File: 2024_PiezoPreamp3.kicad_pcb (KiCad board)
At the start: 4 copper layers, 71 x 36.8 mm, 91 parts, among them J101 6.3mm stereo, J102 6.3mm stereo, J201 DC IN 5.5/2.1mm, J401 Spring Contact, U101 OPA145, U102 OPA145, U201 ZXMP3A17E6TA, U301 BC847BS,115

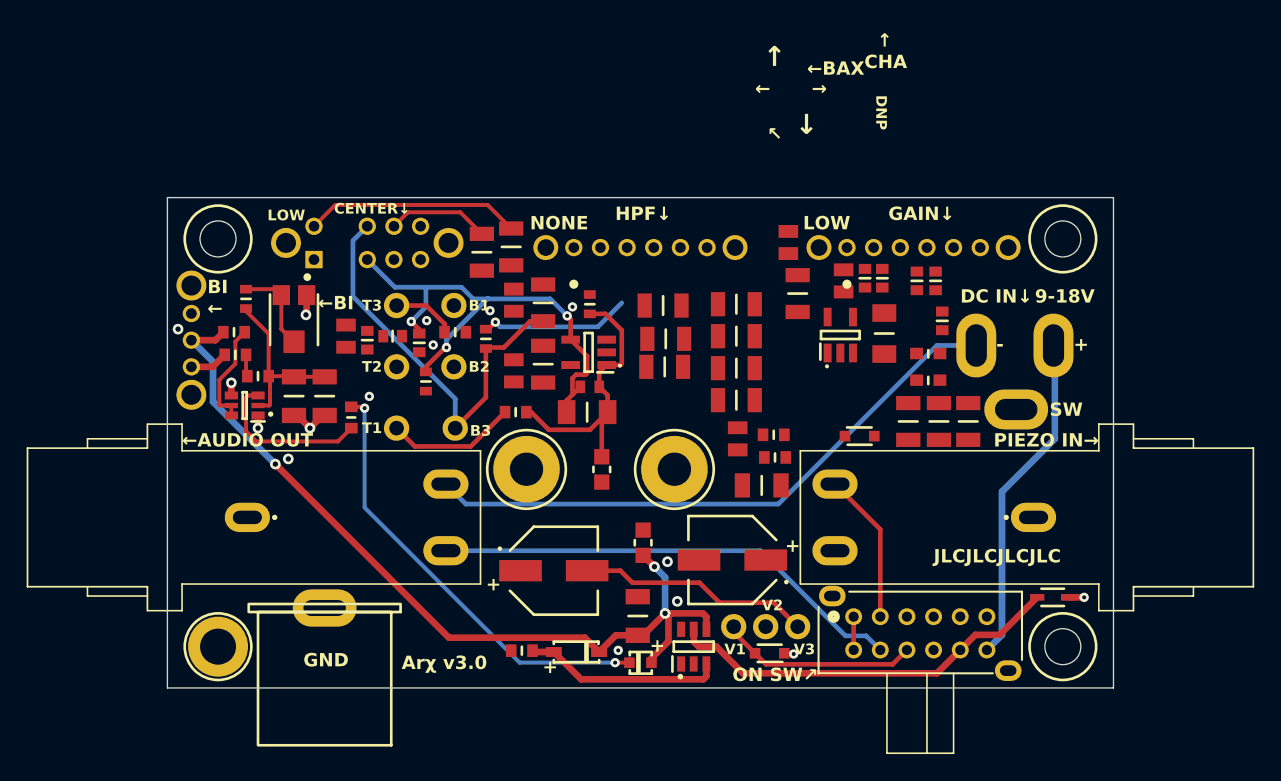
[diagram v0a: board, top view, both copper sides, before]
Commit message: PCB: layout, routing
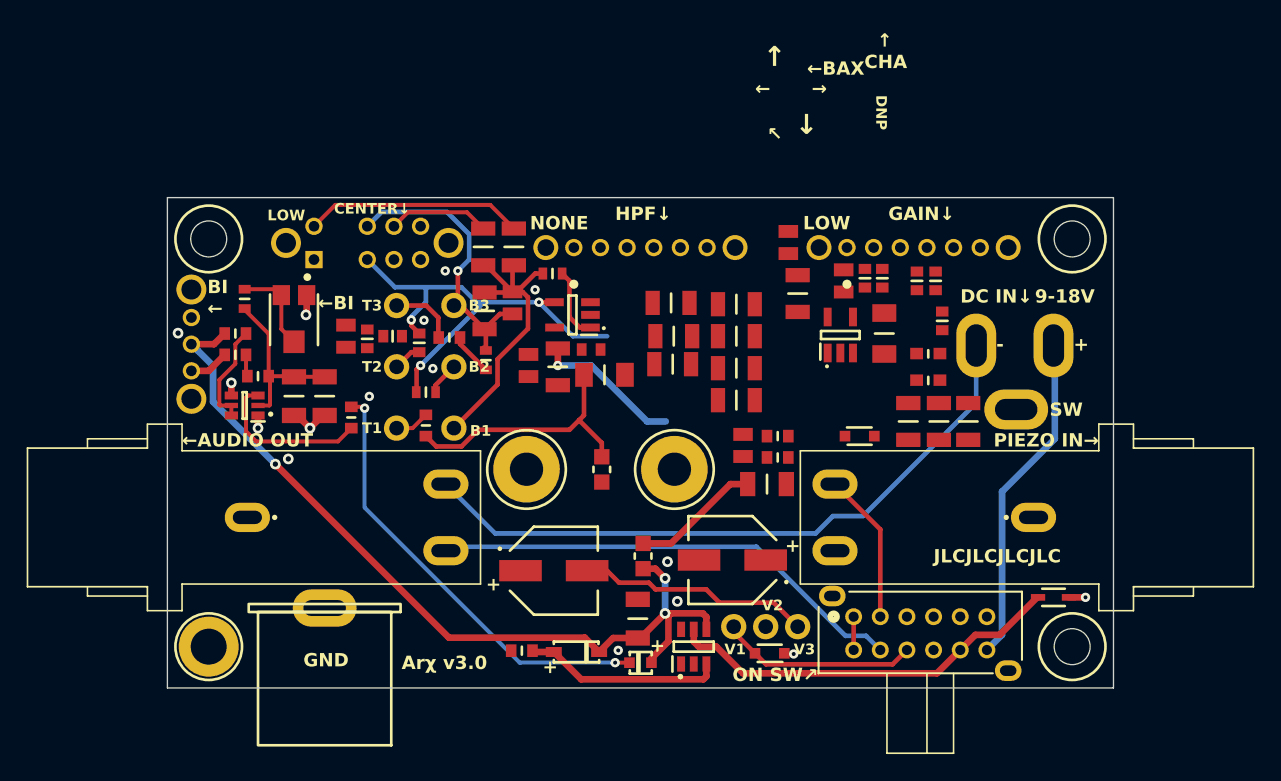
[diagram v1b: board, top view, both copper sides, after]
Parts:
- moved H103 9.20 mm to (136.4, 83.2)
- moved H101 9.20 mm to (136.4, 92.3)
- moved Rt102 6.81 mm to (134.3, 92.2), turned to -90 degrees
- moved Cb101 4.44 mm to (138.7, 83.5)
- moved Rb102 3.62 mm to (143.8, 80.8), turned to 0 degrees
- moved R104 3.09 mm to (147.7, 88.3), turned to 0 degrees
- moved U102 3.06 mm to (145.3, 83.8)
- moved C104 2.80 mm to (146.7, 86.5), turned to 180 degrees
- moved Rb101 1.60 mm to (138.8, 87.2), turned to 90 degrees
- moved C207 1.17 mm to (142.0, 87.7), turned to 90 degrees
- moved C206 1.12 mm to (144.2, 87.8), turned to 90 degrees
- moved R202 1.00 mm to (150.6, 102.0)
- moved R103 0.80 mm to (134.3, 89.7), turned to 180 degrees
- moved H402 0.70 mm to (182.8, 108.8)
- moved H404 0.70 mm to (182.8, 78.2)
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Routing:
- net /1-ChargeAmpAndEQ/BASS_1: track 0.00 -> 23.5 mm
- net VS: track 0.00 -> 20.8 mm, vias 0 -> 1
- net /1-ChargeAmpAndEQ/BASS_3: track 30.8 -> 22.1 mm, vias 0 -> 1
- net /1-ChargeAmpAndEQ/BAX_IN: track 11.3 -> 3.23 mm, vias 1 -> 0
- net /1-ChargeAmpAndEQ/TREB_1: track 9.77 -> 2.61 mm
- net DC_IN_NEG: track 45.4 -> 49.7 mm
- net /1-ChargeAmpAndEQ/BAX_A_OUT: track 21.4 -> 25.0 mm
- net /1-ChargeAmpAndEQ/BAX_A_INV: track 38.2 -> 34.7 mm
- net /1-ChargeAmpAndEQ/BASS_2: track 0.00 -> 2.47 mm
- net /1-ChargeAmpAndEQ/TREB_2: track 0.00 -> 2.16 mm

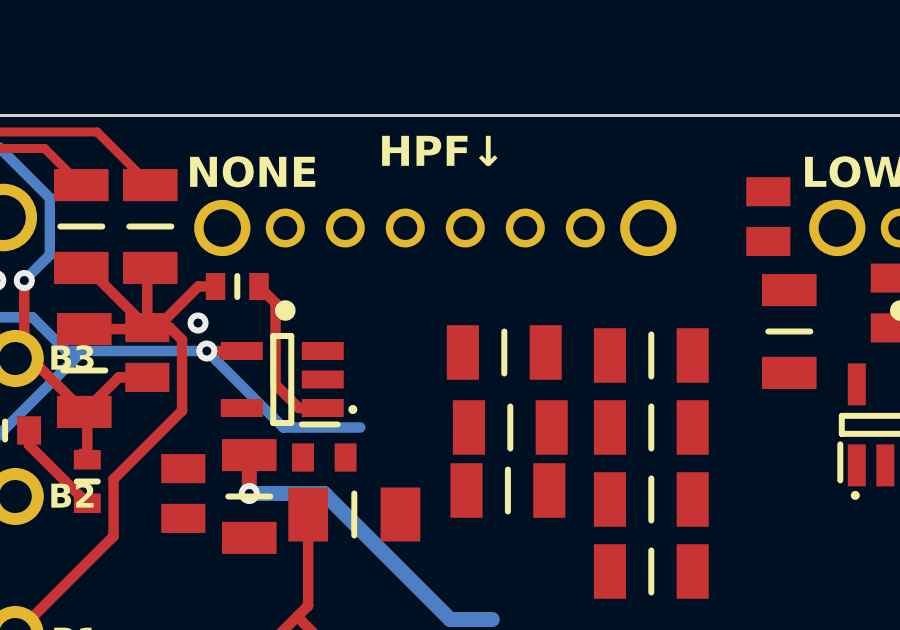
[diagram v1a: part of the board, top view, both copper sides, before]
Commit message: schematic, PCB: defining net classes, assigning different color for Power, getting rid of 0.3493 trace width which was kinda silly anyway
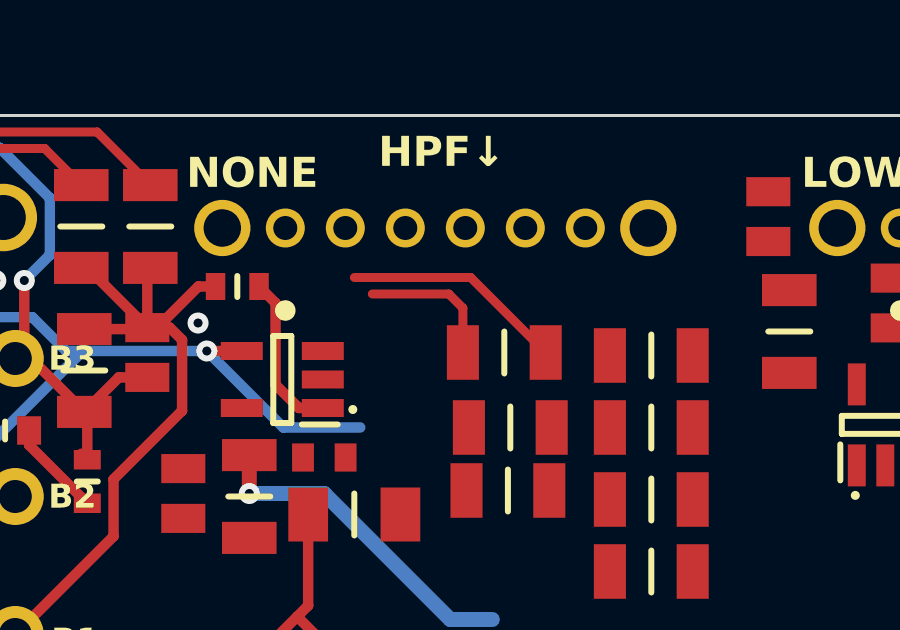
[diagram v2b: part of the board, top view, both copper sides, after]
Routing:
- net /1-ChargeAmpAndEQ/HPF_SW_3: track 0.00 -> 7.42 mm
- net /1-ChargeAmpAndEQ/BAX_IN: track 3.23 -> 7.92 mm
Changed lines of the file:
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@@
 			)
 		)
-		(property "Purpose" "ON/OFF switch for DC + true bypass switch for audio"
+		(property "Purpose" "4PDT. ON/OFF switch for DC + true bypass switch for audio"
 			(at -1.6 -10.7 0)
 			(layer "F.Fab")
@@
 			)
 		)
-		(property "Source" "TME"
+		(property "Source" "Mouser"
 			(at -1.6 -10.7 0)
 			(layer "F.Fab")
@@
 			)
 		)
-		(property "Purpose" "changes the mode of power-on LED. Left = BI, right = LED always on"
+		(property "Purpose" "SPDT. Changes the mode of power-on LED. Left = BI, right = LED always on"
 			(at 0 0 0)
 			(layer "B.Fab")
@@
 			)
 		)
-		(property "Purpose" "sets Baxandall center frequency"
+		(property "Purpose" "DP3T. Sets Baxandall center frequency"
 			(at 0 0 180)
 			(unlocked yes)
@@
 			)
 		)
-		(property "Purpose" "Sets high-pass filter cutoff frequency"
+		(property "Purpose" "SP4T. Sets high-pass filter cutoff frequency"
 			(at -20.3 0.1 180)
 			(unlocked yes)
@@
 			)
 		)
+		(sheetname "1-ChargeAmpAndEQ")
+		(sheetfile "1-ChargeAmpAndEQ.kicad_sch")
 		(attr through_hole exclude_from_pos_files)
 		(fp_line
@@
 			)
 		)
-		(property "Purpose" "Sets gain (ratio of feedback capacitance vs piezo capacitance)"
+		(property "Purpose" "SP4T. Sets gain (ratio of feedback capacitance vs piezo capacitance)"
 			(at -20.3 0.1 180)
 			(unlocked yes)
@@
 			)
 		)
+		(sheetname "1-ChargeAmpAndEQ")
+		(sheetfile "1-ChargeAmpAndEQ.kicad_sch")
 		(attr through_hole exclude_from_pos_files)
 		(fp_line
@@
 	)
 	(segment
+		(start 151.32 82.95)
+		(end 151.32 81.47)
+		(width 0.3)
+		(layer "F.Cu")
+		(net 11)
+	)
+	(segment
+		(start 150.85 81)
+		(end 148.3 81)
+		(width 0.3)
+		(layer "F.Cu")
+		(net 11)
+	)
+	(segment
 		(start 136.86 85.55)
 		(end 136.86 86.035)
@@
 	)
 	(segment
+		(start 151.32 81.47)
+		(end 150.85 81)
+		(width 0.3)
+		(layer "F.Cu")
+		(net 11)
+	)
+	(segment
 		(start 133.9 87.65)
 		(end 133.6 87.95)
@@
 		(net 44)
 	)
+	(segment
+		(start 154.08 82.95)
+		(end 151.58 80.45)
+		(width 0.3)
+		(layer "F.Cu")
+		(net 48)
+	)
+	(segment
+		(start 151.58 80.45)
+		(end 147.7 80.45)
+		(width 0.3)
+		(layer "F.Cu")
+		(net 48)
+	)
 	(zone

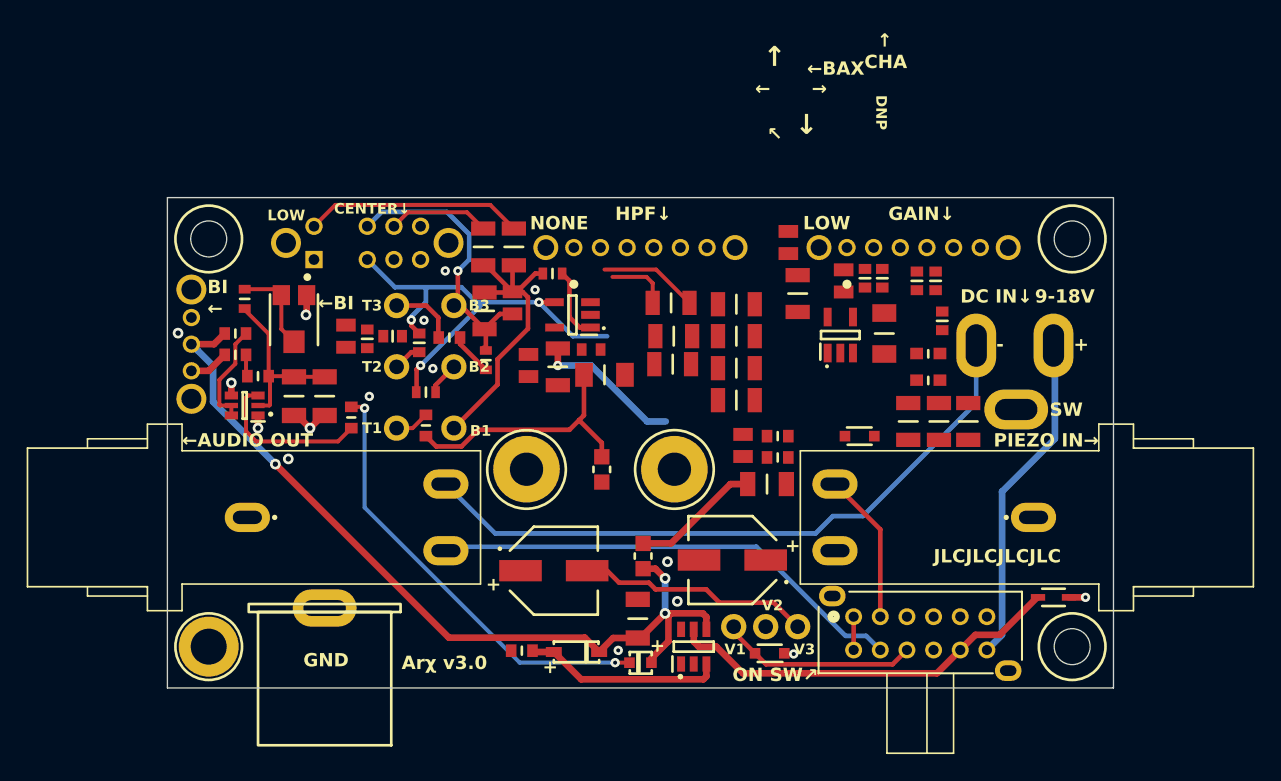
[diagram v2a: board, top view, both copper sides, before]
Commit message: PCB: changing all via sizes to 0.3/0.7 as bigger don't make any sense
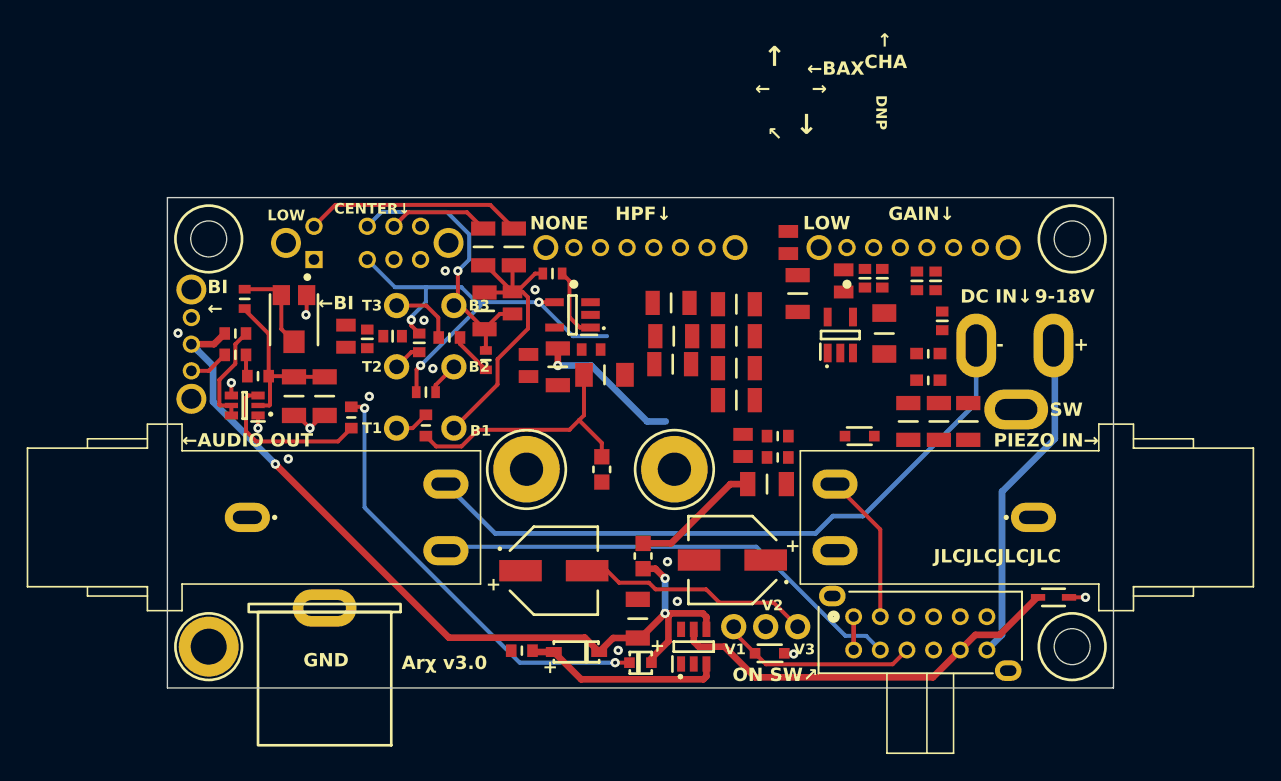
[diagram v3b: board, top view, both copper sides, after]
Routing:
- net /1-ChargeAmpAndEQ/HPF_SW_3: track 7.42 -> 0.00 mm
- net /1-ChargeAmpAndEQ/BAX_IN: track 7.92 -> 3.23 mm
